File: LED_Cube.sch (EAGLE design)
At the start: 19 parts, among them IC1 MSGEQ7SOIC, U1 ATMEGA328P-AU, U2 TLC5940-RHB, U3 TLC5940-RHB, X1 1503_02

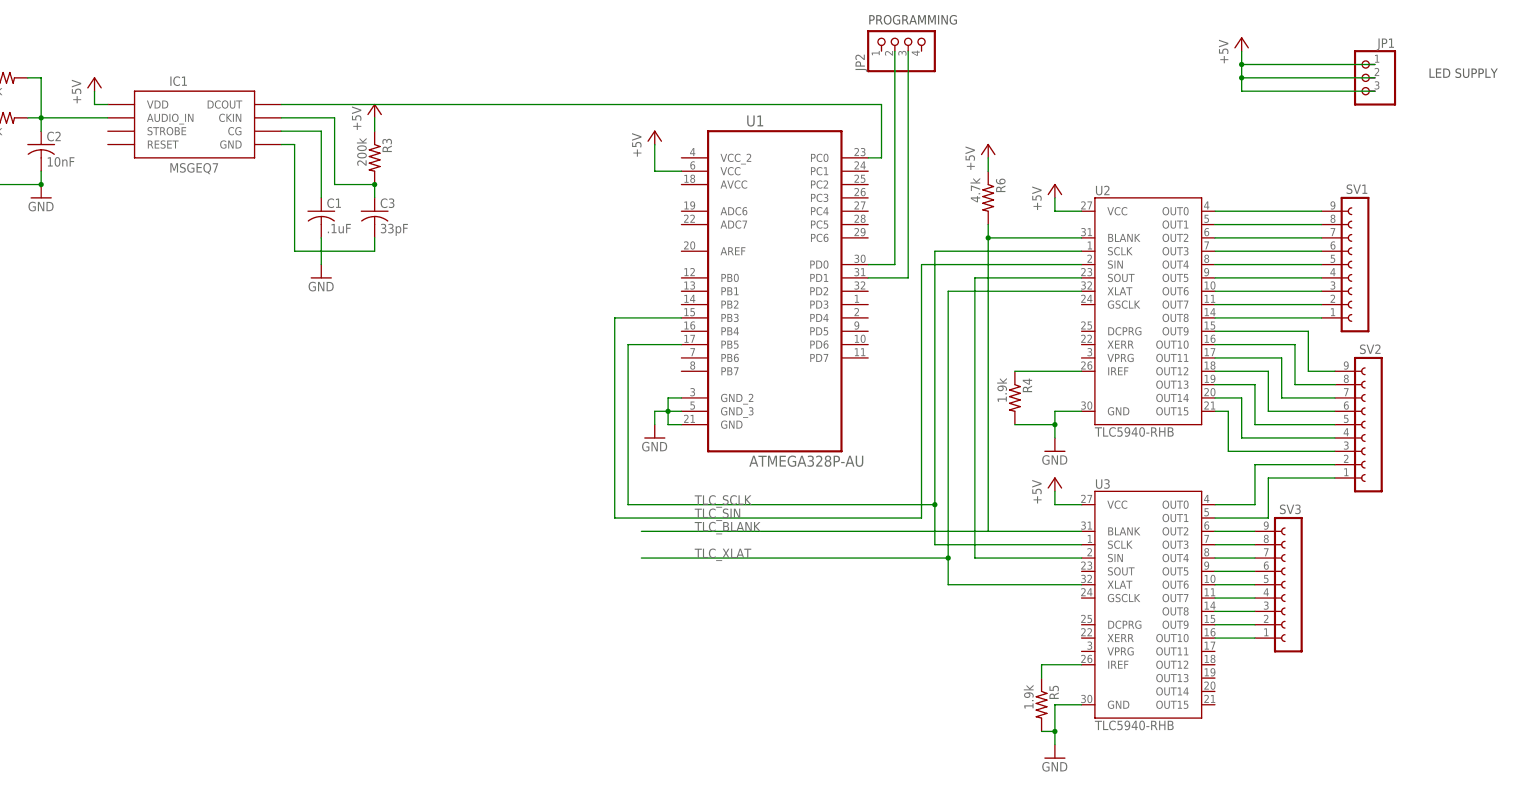
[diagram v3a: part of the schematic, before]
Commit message: further atmega connections
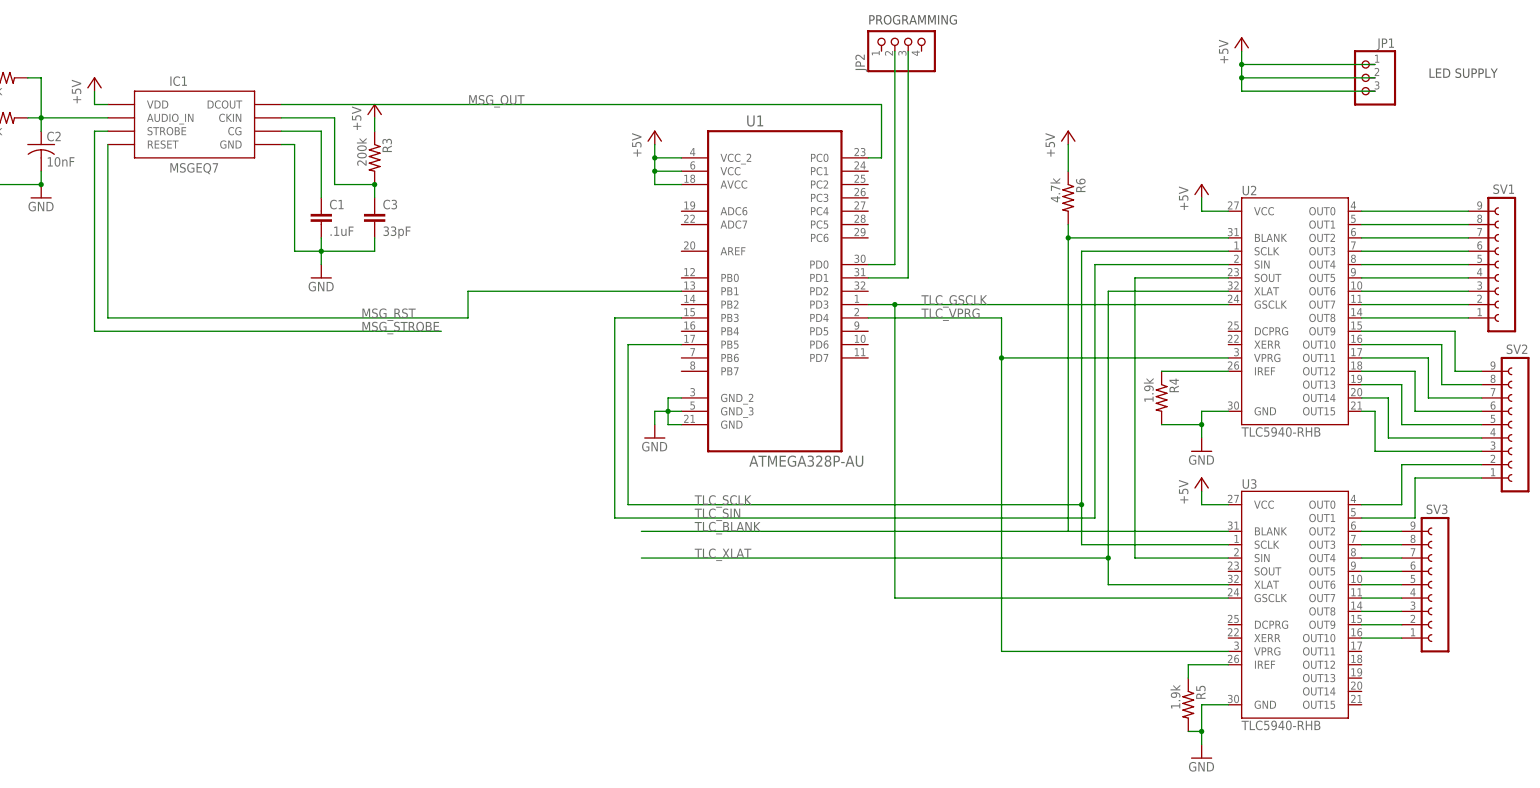
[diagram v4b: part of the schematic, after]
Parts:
- C1, C3: device rcl:C-USC0805 -> rcl:C-EUC0805
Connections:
- net N$36 renamed MSG_OUT
- new net MSG_RST: IC1.RESET, U1.PB1
- new net MSG_STROBE: IC1.STROBE
- new net TLC_GSCLK: U1.PD3, U2.GSCLK, U3.GSCLK
- new net TLC_VPRG: U1.PD4, U2.VPRG, U3.VPRG
- net +5V: now also U1.AVCC, U1.VCC_2
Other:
- moved on the sheet: R4, R5, R6, SV1, SV2, SV3, U2, U3

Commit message: Schematic almost done
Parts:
- added C4: 1uF, rcl:C-EUC0805
- added C5, C6: 22pF, rcl:C-EUC0805
- added JP3: SPI, pinhead:PINHD-2X3
- added JP4: SUPPLY, pinhead:PINHD-1X2
- added Q1: 16MHz, crystal:CRYSTALHC49UP
- JP2: value (none) -> SERIAL
- U2, U3: value TLC5940-RHB -> TLC5940PWP; device SparkFun-DigitalIC:TLC5940-RHB -> SparkFun-DigitalIC:TLC5940PWP
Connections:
- new net N$36: JP3.1, U1.PB4
- new net N$37: JP3.5, U1.PC6
- new net N$38: C5.1, Q1.1, U1.PB6
- new net N$41: C6.1, Q1.2, U1.PB7
- net +5V: now also C4.1, JP2.1, JP3.2, JP4.1
- net GND: now also C4.2, C5.2, C6.2, JP2.4, JP3.6, JP4.2
- net MSG_STROBE: now also U1.PB2
- net TLC_BLANK: now also U1.PD5
- net TLC_SCLK: now also JP3.3
- net TLC_SIN: now also JP3.4
- net TLC_XLAT: now also U1.PD2
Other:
- note removed: "PROGRAMMING"
- moved on the sheet: JP1, JP2, R4, R5, R6, SV1, SV2, SV3, U1, U2, U3

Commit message: more schematic
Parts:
- removed R6: 4.7k, rcl:R-US_R0805
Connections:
- net N$36 renamed SPI_MISO
- net TLC_SCLK renamed SPI_SCLK
- net TLC_SIN renamed SPI_MOSI
- net +5V: no longer R6.1
- net TLC_BLANK: no longer R6.2
- net TLC_XLAT: no longer U3.XLAT
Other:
- moved on the sheet: C1, C3, JP3, R3

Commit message: schematic & board updated
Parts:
- added C10, C11, C12, C13, C7, C9: 1uF, rcl:C-EUC0805
- added C8: 10nF, rcl:C-EUC0805
- added Q2, Q3, Q4: (no value), transistor-power:PMOSFET_PTO220BH
- added R6: 4.7k, rcl:R-US_R0805
- C2: value 10nF -> blocking cap; device rcl:C-USC0805 -> rcl:C-EUC0805
- JP1: value (none) -> LED_SUPPLY
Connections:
- new net LAYER1_OFF: Q4.G, U1.PB0
- new net LAYER2_OFF: Q2.G, U1.PD6
- new net LAYER3_OFF: Q3.G, U1.PD7
- new net N$36: JP1.3, Q3.D
- new net N$42: JP1.2, Q2.D
- new net N$43: JP1.1, Q4.D
- new net N$44: C2.2, IC1.AUDIO_IN
- net +5V: now also C10.1, C11.1, C12.1, C13.1, C7.1, C9.1, Q2.S, Q3.S, Q4.S, R6.2, U1.AREF; no longer JP1.1, JP1.2, JP1.3
- net GND: now also C10.2, C11.2, C12.2, C13.2, C7.2, C8.2, C9.2; no longer C2.2
- net N$37: now also R6.1
- net N$6: now also C8.1; no longer IC1.AUDIO_IN
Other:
- note removed: "LED SUPPLY"
- moved on the sheet: C1, C2, C3, C4, IC1, JP1, JP3, JP4, R1, R2, R3, R4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

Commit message: schematic 80%/board 25%
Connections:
- net LAYER2_OFF: now also Q3.G; no longer Q2.G
- net LAYER3_OFF: now also Q2.G; no longer Q3.G
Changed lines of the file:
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@@
 </segment>
 <segment>
-<pinref part="Q2" gate="G$1" pin="G"/>
-<wire x1="-83.82" y1="5.08" x2="-86.36" y2="5.08" width="0.1524" layer="91"/>
-<label x="-86.36" y="5.08" size="1.778" layer="95" rot="R180" xref="yes"/>
+<pinref part="Q3" gate="G$1" pin="G"/>
+<wire x1="-48.26" y1="5.08" x2="-50.8" y2="5.08" width="0.1524" layer="91"/>
+<label x="-50.8" y="5.08" size="1.778" layer="95" rot="R180" xref="yes"/>
 </segment>
 </net>
@@
 </segment>
 <segment>
-<pinref part="Q3" gate="G$1" pin="G"/>
-<wire x1="-48.26" y1="5.08" x2="-50.8" y2="5.08" width="0.1524" layer="91"/>
-<label x="-50.8" y="5.08" size="1.778" layer="95" rot="R180" xref="yes"/>
+<pinref part="Q2" gate="G$1" pin="G"/>
+<wire x1="-83.82" y1="5.08" x2="-86.36" y2="5.08" width="0.1524" layer="91"/>
+<label x="-86.36" y="5.08" size="1.778" layer="95" rot="R180" xref="yes"/>
 </segment>
 </net>
